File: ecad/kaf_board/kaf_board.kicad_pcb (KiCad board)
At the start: 4 copper layers, 116 x 71 mm, 236 parts, among them J1 PWR, J2 TEC1, J3 Conn_01x12, J4 TEC2, J5 USB, J6 TECPWR, M1 Motor_Servo, M2 Servo cut-out, Q1 MMBT3904LT1G, Q2 NTD4804N, Q3 NTD4804N, U1 MAX4649, U10 LM224, U11 LM224, U12 LM224, U13 LD1117S12CTR_SOT223, U14 LD1117S33CTR_SOT223, U15 MAX743, U16 93LCxxBxxOT, U17 FT2232HL, U18 ICE40HX1K-VQ100, U19 W25X20CL, U2 ADP7118AUJZ, U20 MCP3004, U21 TC4427, U3 AD9826, U4 KAF-CDIP24, U5 TPS7A39, U7 TC4427, U8 TC4427, U9 TC4428, X1 KC7050A-C3, Y1 12 MHz

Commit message: minor changes
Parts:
- C112: value C -> 0.1u
- C25, C32, C33, C34: footprint Capacitors_SMD:C_1812_HandSoldering -> Capacitors_SMD:C_1206_HandSoldering
- C69: footprint Capacitors_Tantalum_SMD:CP_Tantalum_Case-C_EIA-6032-28_Hand -> Capacitors_THT:CP_Radial_D5.0mm_P2.00mm
- moved R30 11.2 mm to (193.0, 87.5), turned to 90 degrees
- moved R35 10.6 mm to (202.0, 103.5), turned to 0 degrees
- moved R28 9.69 mm to (191.0, 87.5), turned to 90 degrees
- moved R29 8.58 mm to (195.5, 87.5), turned to 270 degrees
- moved R34 8.56 mm to (196.0, 103.5), turned to 0 degrees
- moved R31 8.53 mm to (197.2, 87.5), turned to 270 degrees
- moved R32 7.08 mm to (196.0, 105.5), turned to 0 degrees
- moved R33 6.68 mm to (202.0, 105.5), turned to 0 degrees
- moved C45 6.57 mm to (195.0, 97.4)
- moved C46 6.57 mm to (202.6, 97.4)
- moved C47 6.57 mm to (192.8, 97.4)
- moved C48 6.57 mm to (204.8, 97.2)
- moved U11 6.57 mm to (198.8, 97.4)
- moved C69 3.54 mm to (133.0, 70.5)
- moved C41 1.95 mm to (180.9, 127.7), turned to 90 degrees
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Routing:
- net +14.5V: track 64.3 -> 145.2 mm, vias 7 -> 10
- net -14.5V: track 54.9 -> 110.1 mm, vias 7 -> 12
- net /ccd/V_VH: track 8.83 -> 43.2 mm, vias 0 -> 3
- net /ccd/V_VL: track 17.2 -> 41.8 mm, vias 0 -> 1
- net /ccd/VGUARD: track 3.56 -> 24.2 mm, vias 0 -> 2
- net Net-(R30-Pad2): track 5.10 -> 14.5 mm
- net Net-(R28-Pad2): track 5.30 -> 14.0 mm
- net GND: track 186.0 -> 193.9 mm, vias 147 -> 150
- net Net-(R32-Pad2): track 5.69 -> 11.1 mm
- net /power/+15V: track 17.1 -> 19.4 mm
- net /power/-15V: track 13.1 -> 15.1 mm
- net Net-(R34-Pad2): track 5.50 -> 7.42 mm
- net /ccd/V1_3.3V: track 48.9 -> 50.2 mm
- net /fpga/V1_3.3V: track 56.5 -> 57.4 mm
- net /ccd/R_3.3V: track 55.9 -> 56.5 mm

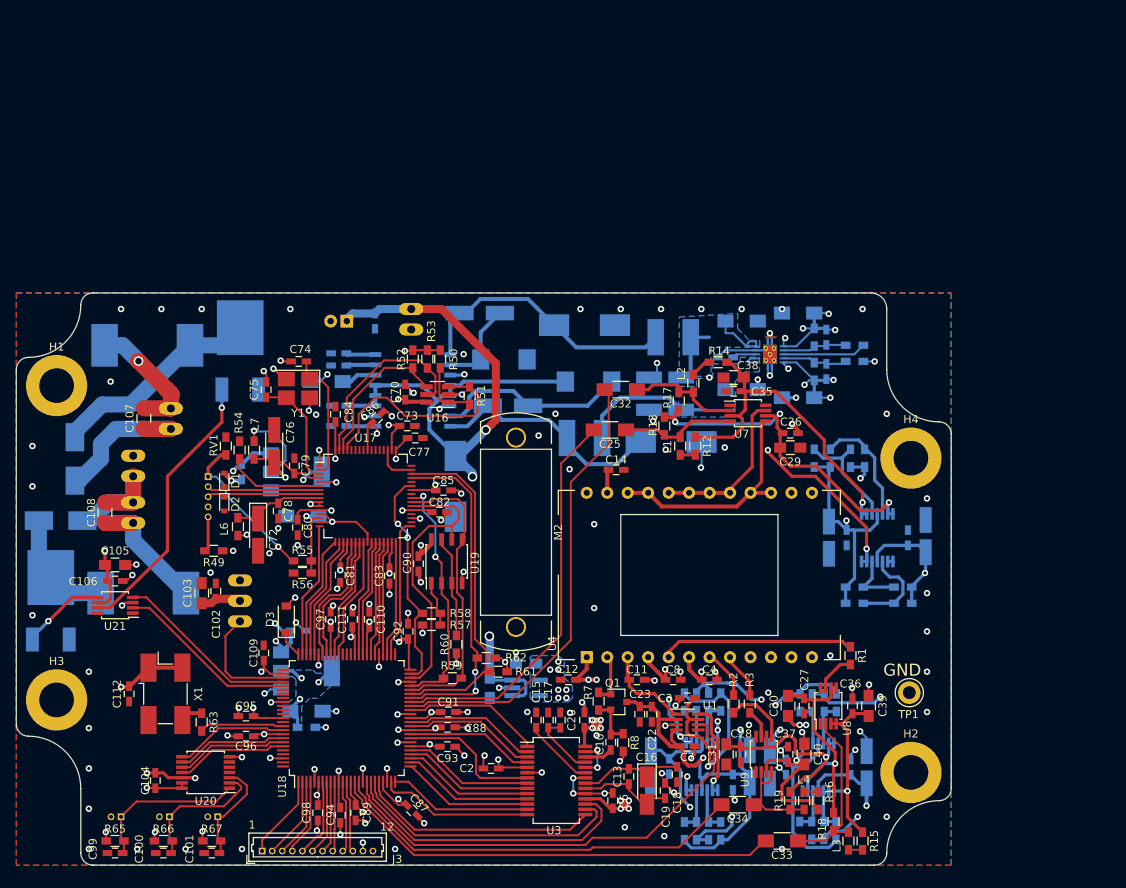
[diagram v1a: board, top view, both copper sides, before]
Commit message: Replaced the MAX743 +-15V converted with another. Not yet routed.
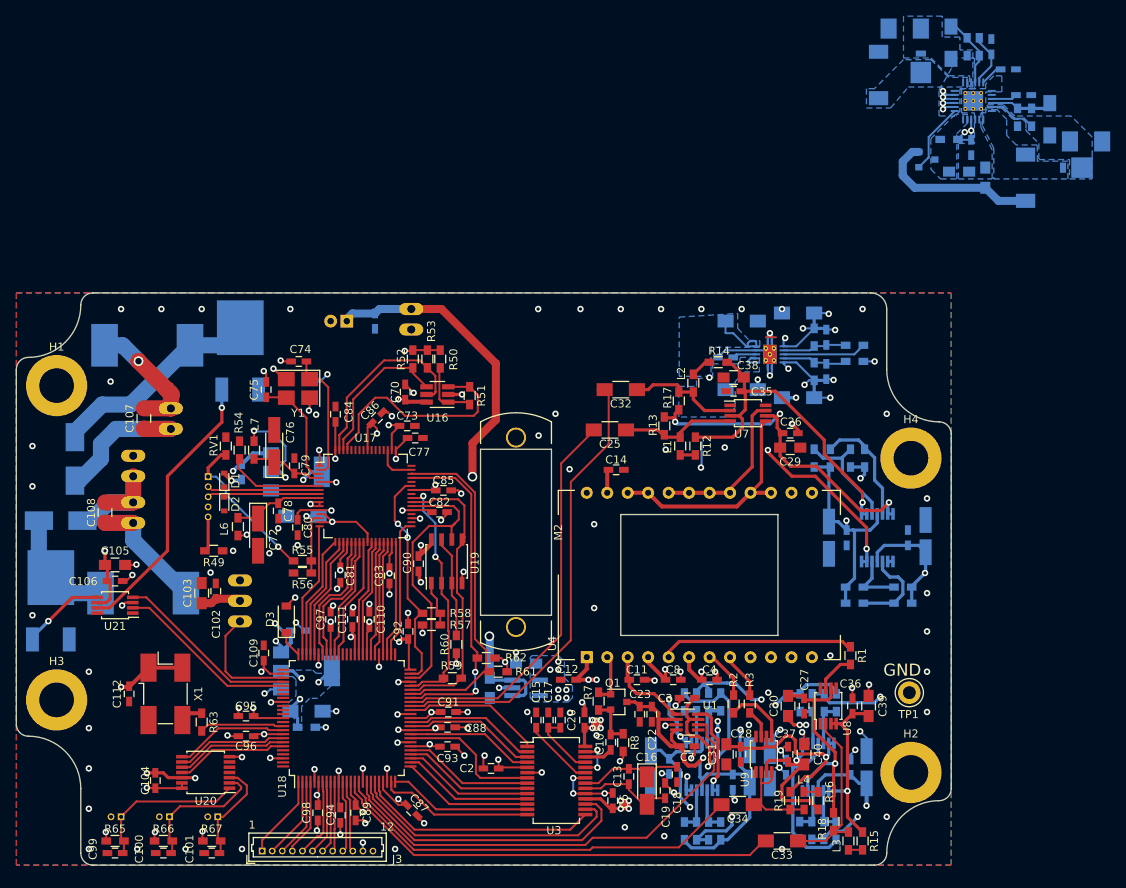
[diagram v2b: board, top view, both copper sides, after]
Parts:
- removed L11, L12: 33u, kaf_board:L_Wuerth_LQS_5040
- removed U15: MAX743, Housings_SOIC:SOIC-16W_7.5x10.3mm_Pitch1.27mm
- added Q4: Si2323DS, TO_SOT_Packages_SMD:SOT-23, B.Cu at (205.0, 50.5)
- added R10: 100, Resistors_SMD:R_0603_HandSoldering, B.Cu at (207.7, 48.0)
- added R11: 104.8k, Resistors_SMD:R_0603_HandSoldering, B.Cu at (211.5, 36.5)
- added R45: 1.3M, Resistors_SMD:R_0603_HandSoldering, B.Cu at (210.0, 36.5)
- added R46: 975k, Resistors_SMD:R_0603_HandSoldering, B.Cu at (218.0, 45.2)
- added R47: 85.8k, Resistors_SMD:R_0603_HandSoldering, B.Cu at (216.2, 45.2)
- added U6: TPS6513x, kaf_board:TI_WQFN-24-1EP_4x4mm_P0.5mm_HandSolder, B.Cu at (210.7, 43.2)
- C53: value 10n -> 4.7u; footprint Capacitors_SMD:C_0603_HandSoldering -> Capacitors_SMD:C_0805_HandSoldering
- C54: value 0.1u -> 4.7u; footprint Capacitors_SMD:C_0603_HandSoldering -> Capacitors_SMD:C_0805_HandSoldering
- C55: value 10u -> 0.1u; footprint Capacitors_SMD:C_1206_HandSoldering -> Capacitors_SMD:C_0603_HandSoldering
- C56: value 1u -> 10n
- C59: value 10n -> 6.8u; footprint Capacitors_SMD:C_0603_HandSoldering -> Capacitors_SMD:C_1206_HandSoldering
- C62: value 100u -> 4.7n; footprint Capacitors_Tantalum_SMD:CP_Tantalum_Case-D_EIA-7343-31_Hand -> Capacitors_SMD:C_0603_HandSoldering
- C63: value 100u -> 220n; footprint Capacitors_Tantalum_SMD:CP_Tantalum_Case-D_EIA-7343-31_Hand -> Capacitors_SMD:C_0603_HandSoldering
- C64: value 100u -> 6.8u; footprint Capacitors_Tantalum_SMD:CP_Tantalum_Case-D_EIA-7343-31_Hand -> Capacitors_SMD:C_1206_HandSoldering
- C65, C66: value 2.2u -> 22u; footprint Capacitors_Tantalum_SMD:CP_Tantalum_Case-A_EIA-3216-18_Hand -> Capacitors_SMD:C_1210_HandSoldering
- D6, D7: value SS14 -> MBRM120; footprint Diodes_SMD:D_SMA_Handsoldering -> Diodes_SMD:D_Powermite_AK
- L10, L5: value 100u -> 4.7u; footprint kaf_board:L_Bourns_SRR0604 -> kaf_board:L_SMT_B82462G4
- R65, R66, R67: value 220 -> 10k
- TH1, TH2, TH3: value 2000, beta 3450 -> 2000, beta 3500
- moved C56 91.4 mm to (217.0, 42.5), turned to 0 degrees
- moved C62 85.9 mm to (215.1, 39.3), turned to 0 degrees
- moved C59 85.2 mm to (208.0, 36.0), turned to 270 degrees
- moved C55 85.1 mm to (210.5, 49.0), turned to 270 degrees
- moved C54 85.1 mm to (212.2, 52.7), turned to 90 degrees
- moved C53 83.2 mm to (209.0, 52.0), turned to 0 degrees
- moved D6 76.5 mm to (223.5, 51.5), turned to 180 degrees
- moved D7 62.7 mm to (204.2, 39.0), turned to 90 degrees
- moved C64 61.7 mm to (220.2, 45.5), turned to 90 degrees
- moved C63 61.2 mm to (213.0, 36.5), turned to 90 degrees
- moved C66 59.9 mm to (224.7, 48.2)
- moved L5 59.8 mm to (217.2, 52.7)
- moved L10 58.4 mm to (199.0, 40.0), turned to 270 degrees
- moved C65 55.9 mm to (202.2, 34.2)
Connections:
- C53 pad 1: Net-(C53-Pad1) -> +6V
- C54 pad 1: +6V -> Net-(C54-Pad1)
- C59 pad 2: GND -> /power/-15V
- C62 pad 1: +6V -> Net-(C62-Pad1)
- C63 pad 1: GND -> Net-(C63-Pad1)
- C63 pad 2: Net-(C63-Pad2) -> GND
- C64 pad 1: Net-(C64-Pad1) -> /power/+15V
- C64 pad 2: GND -> Net-(C64-Pad2)
- C65 pad 1: /power/+15V -> /power/-15V
- C66 pad 1: GND -> /power/+15V
- C66 pad 2: /power/-15V -> GND
- D6 pad 1: Net-(C64-Pad1) -> /power/+15V
- D7 pad 2: Net-(C63-Pad2) -> /power/-15V
- L5 pad 1: +6V -> Net-(D6-Pad2)
- L5 pad 2: Net-(D6-Pad2) -> Net-(C54-Pad1)
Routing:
- net +6V: track 131.8 -> 88.9 mm, vias 6 -> 5
- net Net-(C63-Pad2): track 33.7 -> 0.00 mm
- net Net-(C64-Pad1): track 29.0 -> 0.00 mm
- net Net-(D6-Pad2): track 24.1 -> 0.00 mm
- net Net-(C54-Pad1): track 0.00 -> 20.8 mm
- net /power/+15V: track 19.4 -> 8.24 mm
- net Net-(D7-Pad1): track 10.8 -> 0.00 mm
- net Net-(Q4-Pad1): track 0.00 -> 8.82 mm
- net GND: track 193.9 -> 185.8 mm, vias 150 -> 145
- net Net-(C64-Pad2): track 0.00 -> 7.75 mm
- net Net-(C55-Pad1): track 4.38 -> 11.7 mm, vias 0 -> 6
- net /power/-15V: track 15.1 -> 7.94 mm
- net Net-(C63-Pad1): track 0.00 -> 6.77 mm
- net Net-(C59-Pad1): track 3.66 -> 8.93 mm
- net Net-(C53-Pad1): track 3.62 -> 0.00 mm
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- added copper zone on B.Cu, net +6V
- added copper zone on B.Cu, net Net-(C55-Pad1)
- added copper zone on B.Cu, net Net-(D6-Pad2)
- added copper zone on B.Cu, net Net-(D7-Pad1)

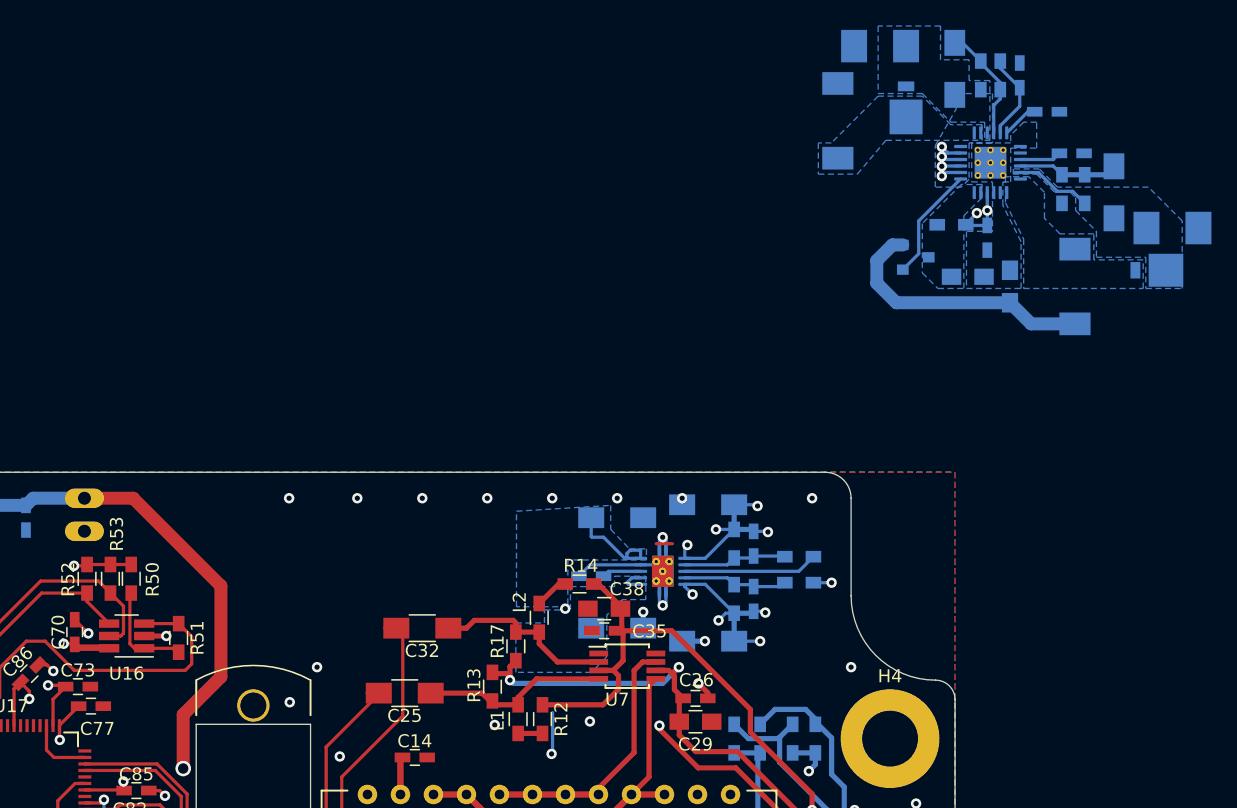
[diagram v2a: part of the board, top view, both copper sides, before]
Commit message: Routed the +-15V converter
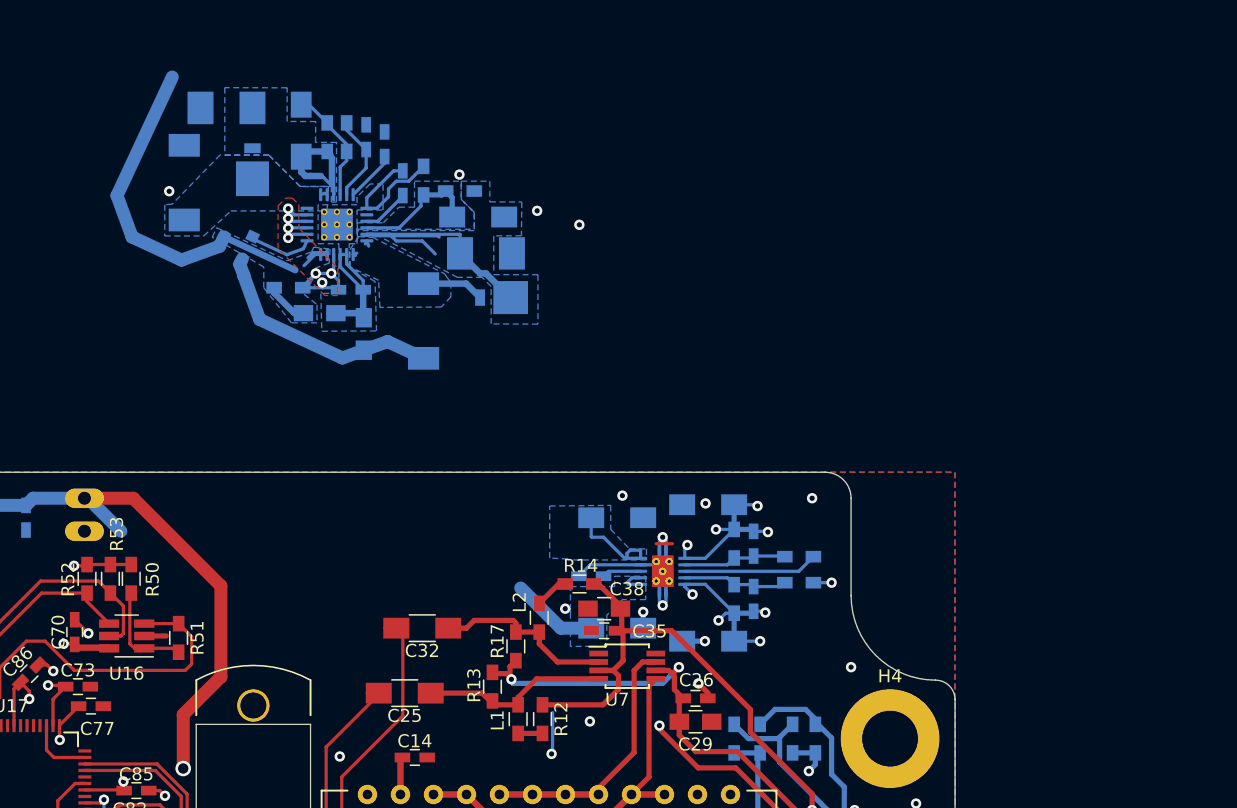
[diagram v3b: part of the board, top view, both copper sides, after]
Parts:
- moved C66 52.9 mm to (171.9, 50.2)
- moved Q4 52.4 mm to (152.6, 49.3), turned to 155 degrees
- moved C56 51.5 mm to (165.5, 44.8), turned to 90 degrees
- moved R10 51.3 mm to (156.7, 52.8)
- moved C62 51.0 mm to (164.1, 41.8), turned to 90 degrees
- moved R11 50.5 mm to (161.2, 41.2)
- moved D7 50.5 mm to (153.9, 43.7)
- moved R45 50.5 mm to (159.7, 41.2)
- moved L10 50.5 mm to (148.7, 44.7)
- moved C59 50.5 mm to (157.7, 40.7)
- moved C63 50.5 mm to (162.7, 41.2)
- moved C65 50.5 mm to (151.9, 39.0)
- moved U6 50.5 mm to (160.4, 47.9)
- moved D6 50.5 mm to (173.1, 53.6)
- moved L5 50.2 mm to (167.1, 55.4)
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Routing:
- net +6V: track 88.9 -> 127.7 mm
- net /power/+15V: track 8.24 -> 34.5 mm
- net GND: track 185.8 -> 208.0 mm, vias 145 -> 140
- net /power/-15V: track 7.94 -> 22.0 mm
- net Net-(D6-Pad2): track 0.00 -> 5.98 mm
- net Net-(Q4-Pad1): track 8.82 -> 4.99 mm
- net Net-(C55-Pad1): track 11.7 -> 15.2 mm, vias 6 -> 7
- net Net-(C54-Pad1): track 20.8 -> 18.7 mm
- net Net-(C64-Pad2): track 7.75 -> 9.75 mm
- net Net-(C62-Pad1): track 2.82 -> 3.88 mm
- net Net-(D7-Pad1): track 0.00 -> 0.54 mm
- added copper zone on F.Cu, net Net-(C55-Pad1)
- added copper zone on B.Cu, net Net-(C64-Pad2)
- removed copper zone on B.Cu, net Net-(C55-Pad1)

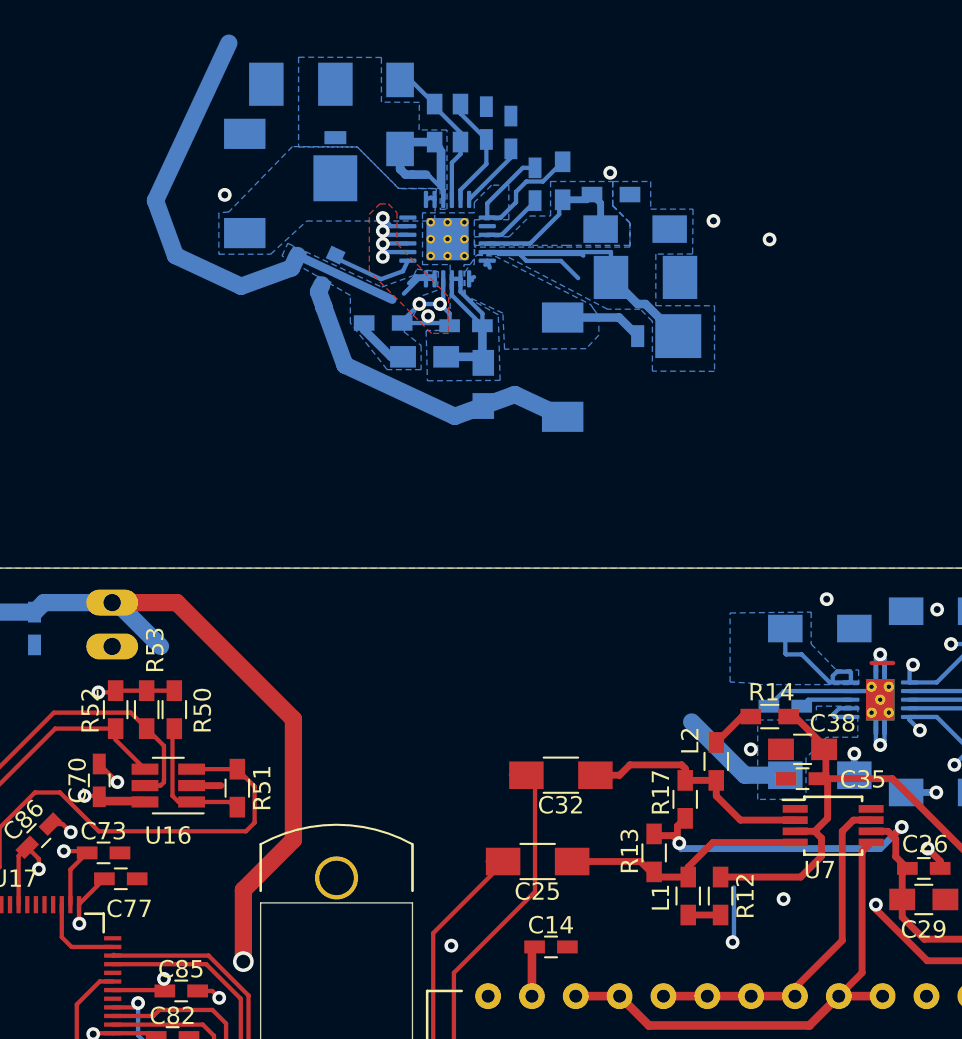
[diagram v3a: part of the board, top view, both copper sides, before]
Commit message: Placed +-15V converter
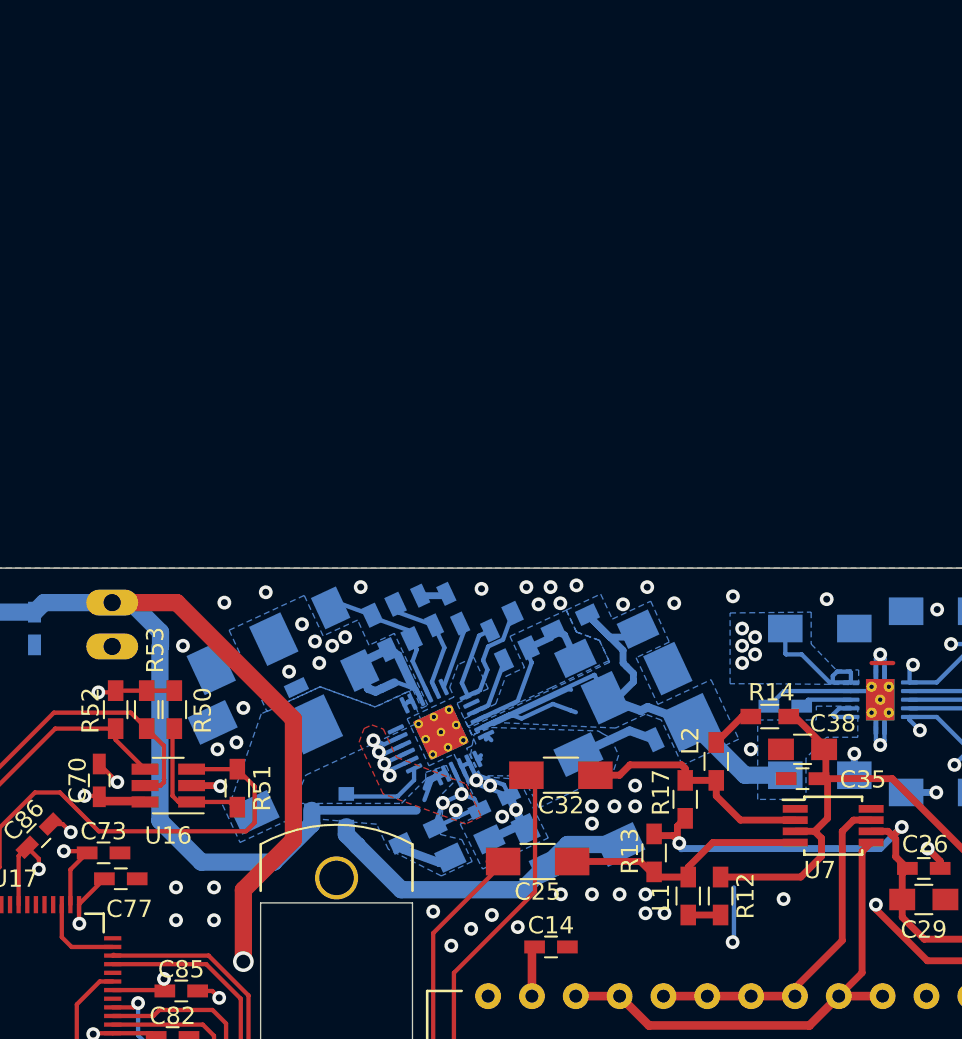
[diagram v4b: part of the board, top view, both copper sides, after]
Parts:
- moved L10 33.8 mm to (148.0, 78.5), turned to 295 degrees
- moved C65 33.2 mm to (148.6, 72.0), turned to 205 degrees
- moved D7 31.7 mm to (152.4, 75.4), turned to 115 degrees
- moved Q4 31.7 mm to (153.6, 81.0), turned to 180 degrees
- moved C59 30.6 mm to (154.5, 71.1), turned to 295 degrees
- moved R10 29.8 mm to (158.7, 82.5), turned to 205 degrees
- moved R45 29.7 mm to (156.5, 70.7), turned to 115 degrees
- moved R11 29.1 mm to (157.9, 70.1), turned to 115 degrees
- moved C53 28.6 mm to (161.7, 83.2), turned to 25 degrees
- moved U6 28.6 mm to (160.0, 76.5), turned to 115 degrees
- moved C63 28.5 mm to (159.2, 69.5), turned to 115 degrees
- moved C62 27.8 mm to (160.8, 69.4), turned to 115 degrees
- moved C55 27.7 mm to (163.1, 80.6), turned to 25 degrees
- moved C54 27.1 mm to (165.5, 83.3), turned to 115 degrees
- moved C56 26.8 mm to (163.3, 71.5), turned to 115 degrees
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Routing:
- net GND: track 208.0 -> 222.2 mm, vias 140 -> 177
- net /power/+15V: track 34.5 -> 45.2 mm
- net /power/-15V: vias 0 -> 11
- added copper zone on In2.Cu, net /power/-15V

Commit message: Last changes before sending PCB to manufacturing
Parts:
- moved C15 0.70 mm to (157.2, 120.0)
- moved Q4 0.68 mm to (154.2, 80.8)
- moved L10 0.64 mm to (147.5, 78.9)
- moved C17 0.60 mm to (158.6, 120.0)
- moved C20 0.50 mm to (160.0, 120.0)
- moved J4 0.50 mm to (106.5, 93.5)
- moved J2 0.38 mm to (111.2, 84.2)
- moved J6 0.35 mm to (106.5, 90.1)
- moved L8 0.25 mm to (108.2, 73.8)
- moved C53 0.20 mm to (161.7, 83.4)
- moved C54 0.20 mm to (165.5, 83.5)
- moved C55 0.20 mm to (163.1, 80.8)
- moved C56 0.20 mm to (163.3, 71.7)
- moved C59 0.20 mm to (154.5, 71.3)
- moved C62 0.20 mm to (160.8, 69.6)
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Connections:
- Q4 pad 2: Net-(C54-Pad1) -> +6V
- Q4 pad 3: +6V -> Net-(C54-Pad1)
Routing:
- net +6V: track 128.2 -> 96.3 mm, vias 5 -> 9
- net GND: track 222.2 -> 217.9 mm, vias 177 -> 205
- net Net-(C54-Pad1): track 18.7 -> 21.2 mm
- net Net-(C64-Pad2): track 9.75 -> 10.9 mm
- net Net-(C17-Pad2): track 8.37 -> 7.29 mm
- net Net-(Q4-Pad1): track 4.99 -> 4.36 mm
- net Net-(C15-Pad1): track 8.76 -> 9.32 mm
- net /thermo_and_mechanical/V_TEC: track 41.0 -> 40.4 mm
- net Net-(C107-Pad2): track 16.9 -> 16.4 mm
- added copper zone on B.Cu, net Net-(C55-Pad1)
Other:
- board text added: "5.2-5.5V"
- board text added: "5.2V"
- board text added: "KAF-CDIP24 v1.0 Mikael Mårtensson"
- board text added: "TEC1"
- board text added: "TEC2"
- board text removed: "5.5-6V"
